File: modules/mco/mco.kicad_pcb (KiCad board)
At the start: 2 copper layers, 30.5 x 68.6 mm, 4 parts

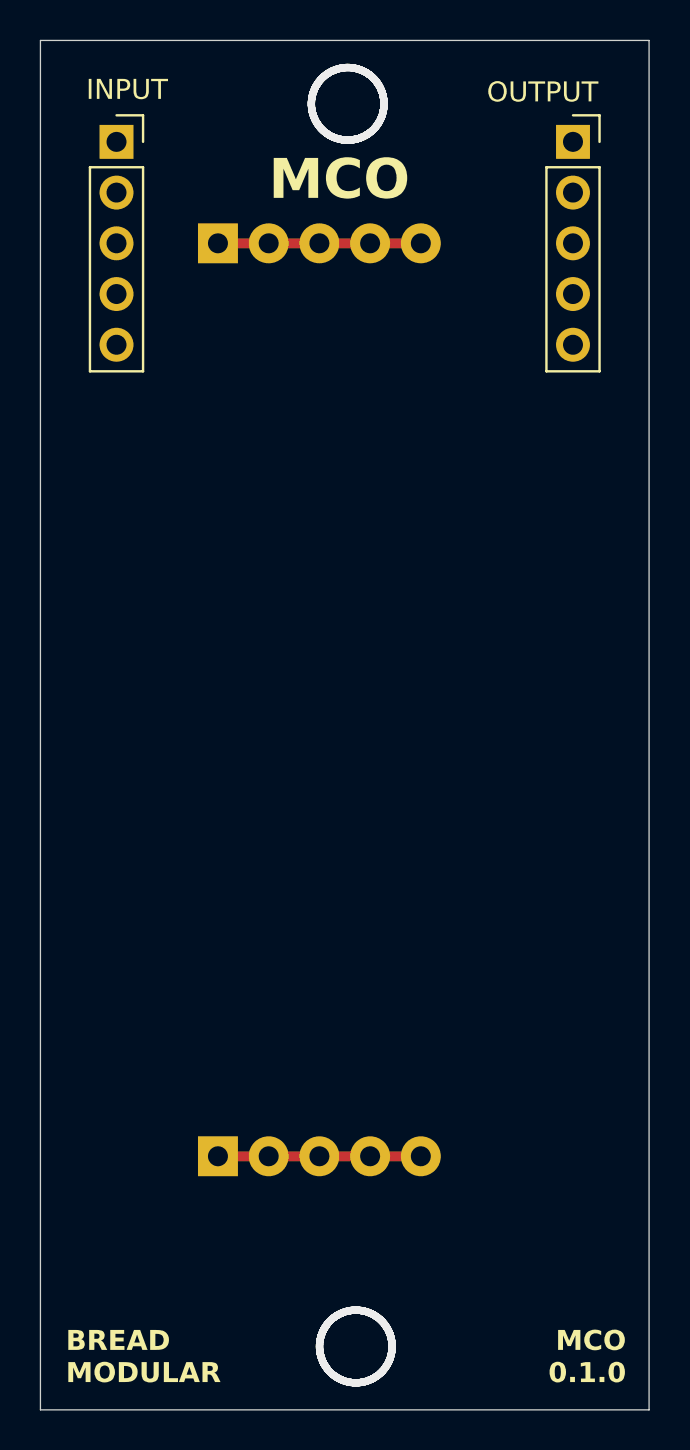
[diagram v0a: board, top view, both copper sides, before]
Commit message: Finalized the PCB design of MCO
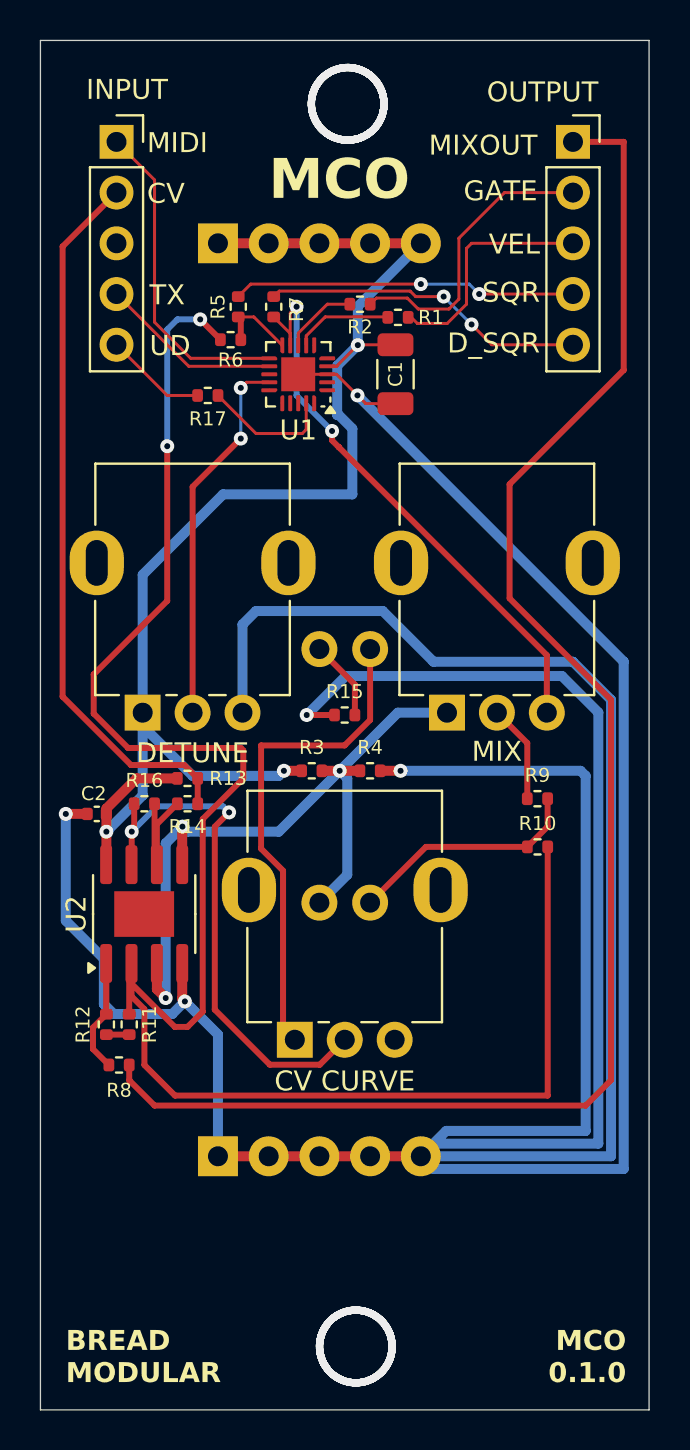
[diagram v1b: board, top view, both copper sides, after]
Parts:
- added C1: 100uf, Capacitor_SMD:C_1206_3216Metric, F.Cu at (64.8, 57.4)
- added C2: 0.1uf, Capacitor_SMD:C_0402_1005Metric, F.Cu at (49.8, 79.4)
- added R1: 1k, Resistor_SMD:R_0402_1005Metric, F.Cu at (64.9, 54.5)
- added R10: 1M, Resistor_SMD:R_0402_1005Metric, F.Cu at (71.9, 81.0)
- added R11: 200k, Resistor_SMD:R_0402_1005Metric, F.Cu at (51.4, 89.9)
- added R12: 200k, Resistor_SMD:R_0402_1005Metric, F.Cu at (50.3, 89.9)
- added R13: 100k, Resistor_SMD:R_0402_1005Metric, F.Cu at (54.4, 77.6)
- added R14: 1M, Resistor_SMD:R_0402_1005Metric, F.Cu at (54.4, 78.9)
- added R15: 510, Resistor_SMD:R_0402_1005Metric, F.Cu at (62.2, 74.4)
- added R16: 1M, Resistor_SMD:R_0402_1005Metric, F.Cu at (52.2, 78.9)
- added R17: 4.7k, Resistor_SMD:R_0402_1005Metric, F.Cu at (55.4, 58.4)
- added R2: 1k, Resistor_SMD:R_0402_1005Metric, F.Cu at (63.0, 53.8)
- added R3: 1k, Resistor_SMD:R_0402_1005Metric, F.Cu at (60.6, 77.2)
- added R4: 1k, Resistor_SMD:R_0402_1005Metric, F.Cu at (63.5, 77.2)
- added R5: 1k, Resistor_SMD:R_0402_1005Metric, F.Cu at (56.9, 54.0)
- added R6: 1M, Resistor_SMD:R_0402_1005Metric, F.Cu at (56.5, 55.6)
- added R7: 1k, Resistor_SMD:R_0402_1005Metric, F.Cu at (58.7, 54.0)
- added R8: 1k, Resistor_SMD:R_0402_1005Metric, F.Cu at (50.9, 91.9)
- added R9: 10k, Resistor_SMD:R_0402_1005Metric, F.Cu at (71.9, 78.6)
- added RV1: 50k, BreadModular_Pots:Potentiometer_RV09, F.Cu at (52.1, 74.3)
- added RV2: 50k, BreadModular_Pots:Potentiometer_RV09, F.Cu at (67.3, 74.3)
- added RV3: 50k, BreadModular_Pots:Potentiometer_RV09, F.Cu at (59.7, 90.7)
- added U1: ATtiny1616-M, Package_DFN_QFN:VQFN-20-1EP_3x3mm_P0.4mm_EP1.7x1.7mm, F.Cu at (59.9, 57.4)
- added U2: MCP6002-xSN, Package_SO:SOIC-8-1EP_3.9x4.9mm_P1.27mm_EP2.29x3mm, F.Cu at (52.2, 84.4)
- added U3: VTL5C, BreadModular_MISC:VTL5C, B.Cu at (62.2, 77.5)
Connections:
- INPUT1 pad 1: unconnected-(INPUT1-Pin_1-Pad1) -> MIDI
- INPUT1 pad 2: unconnected-(INPUT1-Pin_2-Pad2) -> MIX_CV
- INPUT1 pad 4: unconnected-(INPUT1-Pin_4-Pad4) -> TX
- INPUT1 pad 5: unconnected-(INPUT1-Pin_5-Pad5) -> UDPI
- OUTPUT1 pad 1: unconnected-(OUTPUT1-Pin_1-Pad1) -> MIX_OUT
- OUTPUT1 pad 2: unconnected-(OUTPUT1-Pin_2-Pad2) -> GATE
- OUTPUT1 pad 3: unconnected-(OUTPUT1-Pin_3-Pad3) -> VELOCITY
- OUTPUT1 pad 4: unconnected-(OUTPUT1-Pin_4-Pad4) -> SQUARE_OUT
- OUTPUT1 pad 5: unconnected-(OUTPUT1-Pin_5-Pad5) -> DETUNED_OUT
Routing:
- net GND: track 10.2 -> 239.4 mm, vias 0 -> 5
- net Net-(U2A--): track 0.00 -> 93.3 mm, vias 0 -> 2
- net MIX_OUT: track 0.00 -> 79.9 mm
- net V_SUPPLY: track 10.2 -> 71.2 mm, vias 0 -> 3
- net V_MID: track 0.00 -> 37.8 mm, vias 0 -> 3
- net MIX_CV: track 0.00 -> 36.1 mm
- net DETUNED_TONE: track 0.00 -> 29.4 mm, vias 0 -> 2
- net Net-(R16-Pad1): track 0.00 -> 27.0 mm, vias 0 -> 2
- net Net-(U3-+): track 0.00 -> 25.0 mm
- net V_DETUNED: track 0.00 -> 18.8 mm, vias 0 -> 2
- net SQUARE_OUT: track 0.00 -> 17.2 mm, vias 0 -> 2
- net MIDI: track 0.00 -> 16.3 mm
- net DETUNED_OUT: track 0.00 -> 16.2 mm, vias 0 -> 2
- net GATE: track 0.00 -> 14.7 mm
- net Net-(R10-Pad1): track 0.00 -> 11.9 mm
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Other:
- board text added: "CV"
- board text added: "CV CURVE"
- board text added: "DETUNE"
- board text added: "D_SQR"
- board text added: "GATE"
- board text added: "MIDI"
- board text added: "MIX"
- board text added: "MIXOUT"
- board text added: "SQR"
- board text added: "TX"
- board text added: "UD"
- board text added: "VEL"

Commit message: Add mco_0.2.0 schematic
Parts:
- removed C1: 100uf, Capacitor_SMD:C_1206_3216Metric
- removed C2: 0.1uf, Capacitor_SMD:C_0402_1005Metric
- removed R1, R2, R3, R4, R5, R7, R8: 1k, Resistor_SMD:R_0402_1005Metric
- removed R10, R14, R16, R6: 1M, Resistor_SMD:R_0402_1005Metric
- removed R11, R12: 200k, Resistor_SMD:R_0402_1005Metric
- removed R13: 100k, Resistor_SMD:R_0402_1005Metric
- removed R15: 510, Resistor_SMD:R_0402_1005Metric
- removed R17: 4.7k, Resistor_SMD:R_0402_1005Metric
- removed R9: 10k, Resistor_SMD:R_0402_1005Metric
- removed RV1, RV2, RV3: 50k, BreadModular_Pots:Potentiometer_RV09
- removed U1: ATtiny1616-M, Package_DFN_QFN:VQFN-20-1EP_3x3mm_P0.4mm_EP1.7x1.7mm
- removed U2: MCP6002-xSN, Package_SO:SOIC-8-1EP_3.9x4.9mm_P1.27mm_EP2.29x3mm
- removed U3: VTL5C, BreadModular_MISC:VTL5C
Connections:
- INPUT1 pad 1: MIDI -> unconnected-(INPUT1-Pin_1-Pad1)
- INPUT1 pad 2: MIX_CV -> unconnected-(INPUT1-Pin_2-Pad2)
- INPUT1 pad 4: TX -> unconnected-(INPUT1-Pin_4-Pad4)
- INPUT1 pad 5: UDPI -> unconnected-(INPUT1-Pin_5-Pad5)
- OUTPUT1 pad 1: MIX_OUT -> unconnected-(OUTPUT1-Pin_1-Pad1)
- OUTPUT1 pad 2: GATE -> unconnected-(OUTPUT1-Pin_2-Pad2)
- OUTPUT1 pad 3: VELOCITY -> unconnected-(OUTPUT1-Pin_3-Pad3)
- OUTPUT1 pad 4: SQUARE_OUT -> unconnected-(OUTPUT1-Pin_4-Pad4)
- OUTPUT1 pad 5: DETUNED_OUT -> unconnected-(OUTPUT1-Pin_5-Pad5)
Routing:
- net GND: track 239.4 -> 10.2 mm, vias 5 -> 0
- net Net-(U2A--): track 93.3 -> 0.00 mm, vias 2 -> 0
- net MIX_OUT: track 79.9 -> 0.00 mm
- net V_SUPPLY: track 71.2 -> 10.2 mm, vias 3 -> 0
- net V_MID: track 37.8 -> 0.00 mm, vias 3 -> 0
- net MIX_CV: track 36.1 -> 0.00 mm
- net DETUNED_TONE: track 29.4 -> 0.00 mm, vias 2 -> 0
- net Net-(R16-Pad1): track 27.0 -> 0.00 mm, vias 2 -> 0
- net Net-(U3-+): track 25.0 -> 0.00 mm
- net V_DETUNED: track 18.8 -> 0.00 mm, vias 2 -> 0
- net SQUARE_OUT: track 17.2 -> 0.00 mm, vias 2 -> 0
- net MIDI: track 16.3 -> 0.00 mm
- net DETUNED_OUT: track 16.2 -> 0.00 mm, vias 2 -> 0
- net GATE: track 14.7 -> 0.00 mm
- net Net-(R10-Pad1): track 11.9 -> 0.00 mm
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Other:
- board text added: "NAME"
- board text added: "NAME 0.0.0"
- board text removed: "CV"
- board text removed: "CV CURVE"
- board text removed: "DETUNE"
- board text removed: "D_SQR"
- board text removed: "GATE"
- board text removed: "MCO"
- board text removed: "MCO 0.1.0"
- board text removed: "MIDI"
- board text removed: "MIX"
- board text removed: "MIXOUT"
- board text removed: "SQR"
- board text removed: "TX"
- board text removed: "UD"
- board text removed: "VEL"

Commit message: finalized the PCB design
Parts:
- added C1: 100uf, Capacitor_SMD:C_1206_3216Metric, F.Cu at (59.5, 88.0)
- added C2: 100nf, Capacitor_SMD:C_0402_1005Metric, F.Cu at (60.7, 90.7)
- added C3: 0.1uf, Capacitor_SMD:C_0402_1005Metric, F.Cu at (66.5, 61.5)
- added C4: 0.1uf, Capacitor_SMD:C_0402_1005Metric, F.Cu at (60.5, 54.2)
- added D1: LED, LED_SMD:LED_0603_1608Metric, F.Cu at (51.3, 80.0)
- added R1: 4.7k, Resistor_SMD:R_0402_1005Metric, F.Cu at (50.7, 60.5)
- added R2: 1k, Resistor_SMD:R_0402_1005Metric, F.Cu at (64.8, 54.1)
- added R3: 1k, Resistor_SMD:R_0402_1005Metric, F.Cu at (73.9, 60.5)
- added R4: 1k, Resistor_SMD:R_0402_1005Metric, F.Cu at (56.5, 92.5)
- added R5: 1k, Resistor_SMD:R_0402_1005Metric, F.Cu at (58.9, 92.5)
- added R6: 330, Resistor_SMD:R_0402_1005Metric, F.Cu at (54.1, 80.0)
- added R7: 100k, Resistor_SMD:R_0402_1005Metric, F.Cu at (54.1, 61.6)
- added R8: 100k, Resistor_SMD:R_0402_1005Metric, F.Cu at (61.5, 61.6)
- added RV1: 50k, BreadModular_Pots:Potentiometer_RV09, F.Cu at (69.2, 84.5)
- added RV2: 1M, BreadModular_Pots:Potentiometer_RV09, F.Cu at (55.4, 67.9)
- added RV3: 1M, BreadModular_Pots:Potentiometer_RV09, F.Cu at (69.3, 67.9)
- added SW1: MODE SELECT, BreadModular_MISC:SPST_TS-1187A-B-A-B, F.Cu at (52.1, 87.0)
- added U1: MCP6002-xSN, Package_SO:SOIC-8-1EP_3.9x4.9mm_P1.27mm_EP2.29x3mm, F.Cu at (67.4, 57.8)
- added U2: ATtiny1616-M, Package_DFN_QFN:VQFN-20-1EP_3x3mm_P0.4mm_EP1.7x1.7mm, F.Cu at (59.5, 82.8)
- added U3: MCP6002-xSN, Package_SO:SOIC-8-1EP_3.9x4.9mm_P1.27mm_EP2.29x3mm, F.Cu at (57.7, 57.8)
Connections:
- INPUT1 pad 1: unconnected-(INPUT1-Pin_1-Pad1) -> MIDI
- INPUT1 pad 2: unconnected-(INPUT1-Pin_2-Pad2) -> CV1
- INPUT1 pad 3: unconnected-(INPUT1-Pin_3-Pad3) -> CV2
- INPUT1 pad 4: unconnected-(INPUT1-Pin_4-Pad4) -> TX
- INPUT1 pad 5: unconnected-(INPUT1-Pin_5-Pad5) -> UDPI
- OUTPUT1 pad 1: unconnected-(OUTPUT1-Pin_1-Pad1) -> AUDIO_OUT
- OUTPUT1 pad 2: unconnected-(OUTPUT1-Pin_2-Pad2) -> AUDIO_OUT
- OUTPUT1 pad 3: unconnected-(OUTPUT1-Pin_3-Pad3) -> AUDIO_OUT
- OUTPUT1 pad 4: unconnected-(OUTPUT1-Pin_4-Pad4) -> GATE_OUT
- OUTPUT1 pad 5: unconnected-(OUTPUT1-Pin_5-Pad5) -> GATE_OUT
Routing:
- net GND: track 10.2 -> 210.3 mm, vias 0 -> 7
- net V_SUPPLY: track 10.2 -> 103.1 mm, vias 0 -> 6
- net Net-(U1A-+): track 0.00 -> 51.2 mm, vias 0 -> 2
- net MIDI: track 0.00 -> 48.7 mm
- net TX: track 0.00 -> 43.6 mm
- net Net-(U2-~{RESET}/PA0): track 0.00 -> 38.8 mm, vias 0 -> 2
- net Net-(U1B-+): track 0.00 -> 37.0 mm, vias 0 -> 2
- net CV2: track 0.00 -> 25.2 mm
- net Net-(U3A--): track 0.00 -> 24.2 mm, vias 0 -> 2
- net Net-(U3B--): track 0.00 -> 23.1 mm
- net BUFF_CV2: track 0.00 -> 20.6 mm, vias 0 -> 2
- net CV1: track 0.00 -> 17.3 mm
- net AUDIO_OUT: track 0.00 -> 14.8 mm
- net Net-(SW1-B): track 0.00 -> 12.8 mm, vias 0 -> 2
- net BUFF_CV1: track 0.00 -> 12.1 mm, vias 0 -> 2
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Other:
- board text added: "AUDIO"
- board text added: "CV1"
- board text added: "CV2"
- board text added: "GATE"
- board text added: "LOWPASS"
- board text added: "MCO"
- board text added: "MCO 0.2.0"
- board text added: "MIDI"
- board text added: "MODE"
- board text added: "TX"
- board text added: "U"
- board text removed: "NAME"
- board text removed: "NAME 0.0.0"

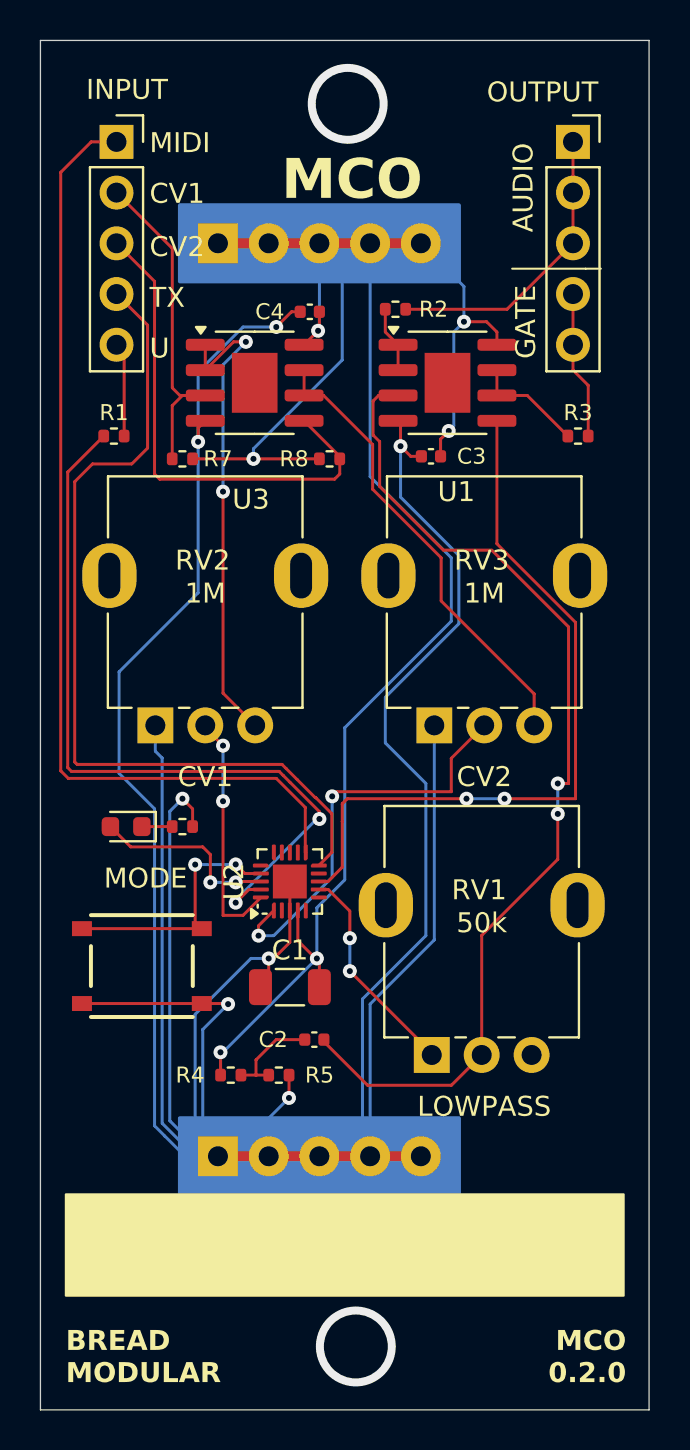
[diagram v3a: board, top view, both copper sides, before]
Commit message: mco: Rebrand the 0.1.0 version as the new MCO. We removed CV support and it's not needed.
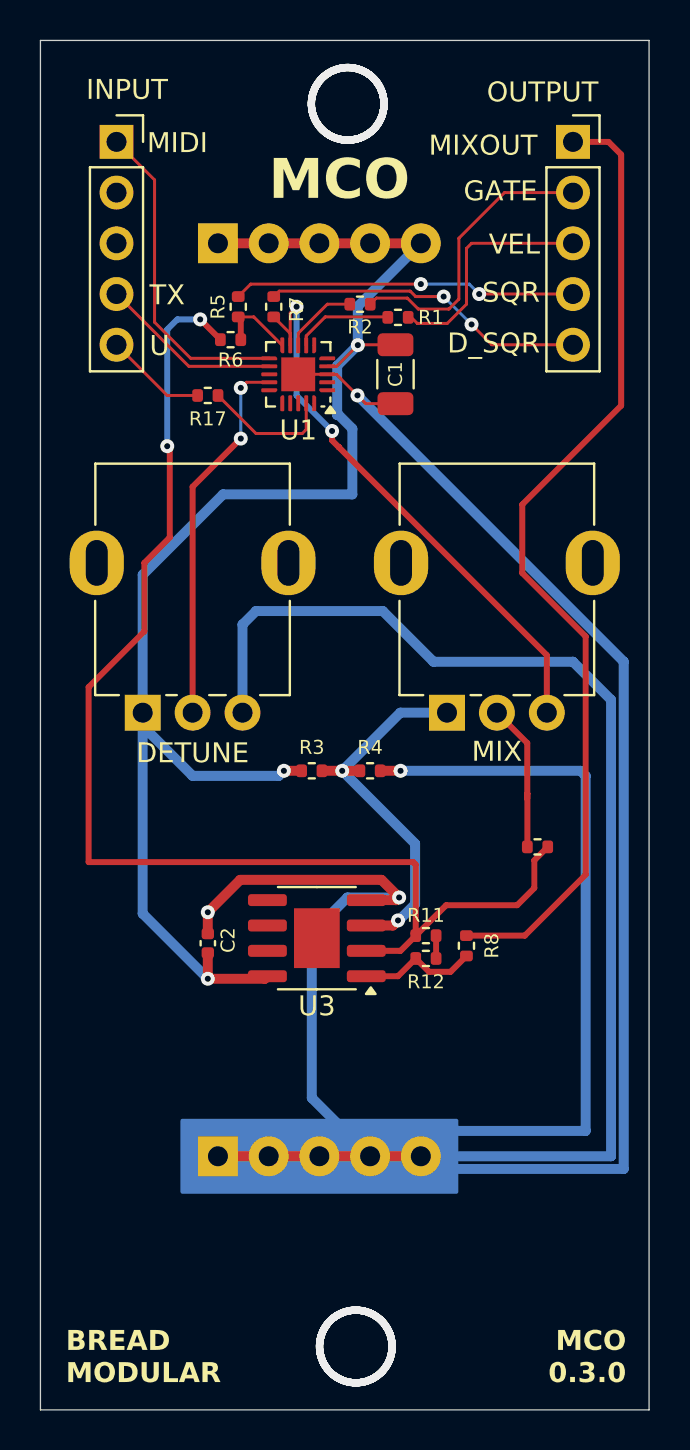
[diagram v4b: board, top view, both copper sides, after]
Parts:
- removed C3, C4: 0.1uf, Capacitor_SMD:C_0402_1005Metric
- removed D1: LED, LED_SMD:LED_0603_1608Metric
- removed RV3: 1M, BreadModular_Pots:Potentiometer_RV09
- removed SW1: MODE SELECT, BreadModular_MISC:SPST_TS-1187A-B-A-B
- removed U2: ATtiny1616-M, Package_DFN_QFN:VQFN-20-1EP_3x3mm_P0.4mm_EP1.7x1.7mm
- added R10: 1M, Resistor_SMD:R_0402_1005Metric, F.Cu at (71.9, 81.0)
- added R11: 200k, Resistor_SMD:R_0402_1005Metric, F.Cu at (66.3, 85.5)
- added R12: 200k, Resistor_SMD:R_0402_1005Metric, F.Cu at (66.3, 86.6)
- added R17: 4.7k, Resistor_SMD:R_0402_1005Metric, F.Cu at (55.4, 58.4)
- C2: value 100nf -> 0.1uf
- R1: value 4.7k -> 1k
- R6: value 330 -> 1M
- R7, R8: value 100k -> 1k
- RV2: value 1M -> 50k
- U1: value MCP6002-xSN -> ATtiny1616-M; footprint Package_SO:SOIC-8-1EP_3.9x4.9mm_P1.27mm_EP2.29x3mm -> Package_DFN_QFN:VQFN-20-1EP_3x3mm_P0.4mm_EP1.7x1.7mm
- moved R5 38.5 mm to (56.9, 54.0), turned to 90 degrees
- moved C1 31.1 mm to (64.8, 57.4), turned to 90 degrees
- moved U3 28.0 mm to (60.8, 85.6), turned to 180 degrees
- moved R8 25.3 mm to (68.3, 86.0), turned to 90 degrees
- moved R6 24.5 mm to (56.5, 55.6), turned to 180 degrees
- moved R3 21.4 mm to (60.6, 77.2)
- moved RV1 19.9 mm to (52.1, 74.3), turned to 90 degrees
- moved R4 16.8 mm to (63.5, 77.2)
- moved R1 15.4 mm to (64.9, 54.5)
- moved RV2 13.6 mm to (67.3, 74.3), turned to 90 degrees
- moved R7 8.88 mm to (58.7, 54.0), turned to 90 degrees
- moved U1 7.49 mm to (59.9, 57.4), turned to 180 degrees
- moved C2 7.19 mm to (55.4, 85.9), turned to 90 degrees
- moved R2 1.79 mm to (63.0, 53.8)
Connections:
- C2 pad 1: V_MID -> V_SUPPLY
- C2 pad 2: Net-(U1A-+) -> GND
- INPUT1 pad 2: CV1 -> unconnected-(INPUT1-Pin_2-Pad2)
- INPUT1 pad 3: CV2 -> unconnected-(INPUT1-Pin_3-Pad3)
- OUTPUT1 pad 1: AUDIO_OUT -> MIX_OUT
- OUTPUT1 pad 2: AUDIO_OUT -> GATE
- OUTPUT1 pad 3: AUDIO_OUT -> VELOCITY
- OUTPUT1 pad 4: GATE_OUT -> SQUARE_OUT
- OUTPUT1 pad 5: GATE_OUT -> DETUNED_OUT
- R1 pad 1: Net-(U2-~{RESET}/PA0) -> Net-(U1-PA6)
- R1 pad 2: UDPI -> VELOCITY
- R2 pad 1: Net-(U1A--) -> Net-(U1-PA7)
- R2 pad 2: AUDIO_OUT -> GATE
- R3 pad 1: Net-(U1B--) -> V_SUPPLY
- R3 pad 2: GATE_OUT -> V_MID
- R4 pad 1: V_SUPPLY -> V_MID
- R4 pad 2: V_MID -> GND
- R5 pad 1: V_MID -> FUNDAMENTAL_TONE
- R5 pad 2: GND -> SQUARE_OUT
- R6 pad 1: Net-(D1-K) -> FUNDAMENTAL_TONE
- R6 pad 2: GND -> Net-(U3A--)
- R7 pad 1: V_SUPPLY -> DETUNED_TONE
- R7 pad 2: CV1 -> DETUNED_OUT
- R8 pad 1: V_SUPPLY -> Net-(R12-Pad2)
- R8 pad 2: CV2 -> MIX_OUT
- RV1 pad 1: Net-(U2-PA6) -> V_SUPPLY
- RV1 pad 2: Net-(U1A-+) -> V_DETUNED
- RV1 pad 3: unconnected-(RV1-Pad3) -> GND
- RV2 pad 1: GND -> V_MID
- RV2 pad 2: BUFF_CV1 -> Net-(R10-Pad1)
- RV2 pad 3: Net-(U3A--) -> DETUNED_TONE
- U1 pad 1: Net-(U1A--) -> unconnected-(U1-PA2-Pad1)
- U1 pad 2: Net-(U1A--) -> unconnected-(U1-PA3-Pad2)
- U1 pad 3: Net-(U1A-+) -> GND
- U1 pad 4: GND -> V_SUPPLY
- U1 pad 5: Net-(U1B-+) -> unconnected-(U1-PA4-Pad5)
- U1 pad 6: Net-(U1B--) -> unconnected-(U1-PA5-Pad6)
- U1 pad 7: Net-(U1B--) -> Net-(U1-PA6)
- U1 pad 8: V_SUPPLY -> Net-(U1-PA7)
- U1 pad 9: (no net) -> DETUNED_TONE
- U3 pad 1: Net-(U3A--) -> Net-(R12-Pad2)
- U3 pad 3: CV1 -> V_MID
- U3 pad 5: CV2 -> unconnected-(U3B-+-Pad5)
- U3 pad 6: Net-(U3B--) -> unconnected-(U3B---Pad6)
- U3 pad 7: Net-(U3B--) -> unconnected-(U3-Pad7)
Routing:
- net Net-(U1A-+): track 51.2 -> 0.00 mm, vias 2 -> 0
- net MIX_OUT: track 0.00 -> 49.3 mm
- net Net-(U3A--): track 24.2 -> 63.9 mm
- net Net-(U2-~{RESET}/PA0): track 38.8 -> 0.00 mm, vias 2 -> 0
- net Net-(U1B-+): track 37.0 -> 0.00 mm, vias 2 -> 0
- net TX: track 43.6 -> 9.15 mm
- net MIDI: track 48.7 -> 16.3 mm
- net DETUNED_TONE: track 0.00 -> 29.4 mm, vias 0 -> 2
- net V_SUPPLY: track 103.1 -> 76.6 mm, vias 6 -> 3
- net CV2: track 25.2 -> 0.00 mm
- net Net-(U3B--): track 23.1 -> 0.00 mm
- net BUFF_CV2: track 20.6 -> 0.00 mm, vias 2 -> 0
- net V_DETUNED: track 0.00 -> 18.8 mm, vias 0 -> 2
- net CV1: track 17.3 -> 0.00 mm
- net SQUARE_OUT: track 0.00 -> 17.2 mm, vias 0 -> 2
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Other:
- board text added: "DETUNE"
- board text added: "D_SQR"
- board text added: "MCO 0.3.0"
- board text added: "MIX"
- board text added: "MIXOUT"
- board text added: "SQR"
- board text added: "VEL"
- board text removed: "AUDIO"
- board text removed: "CV1"
- board text removed: "CV2"
- board text removed: "LOWPASS"
- board text removed: "MCO 0.2.0"
- board text removed: "MODE"
